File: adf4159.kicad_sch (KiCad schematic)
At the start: 0 parts

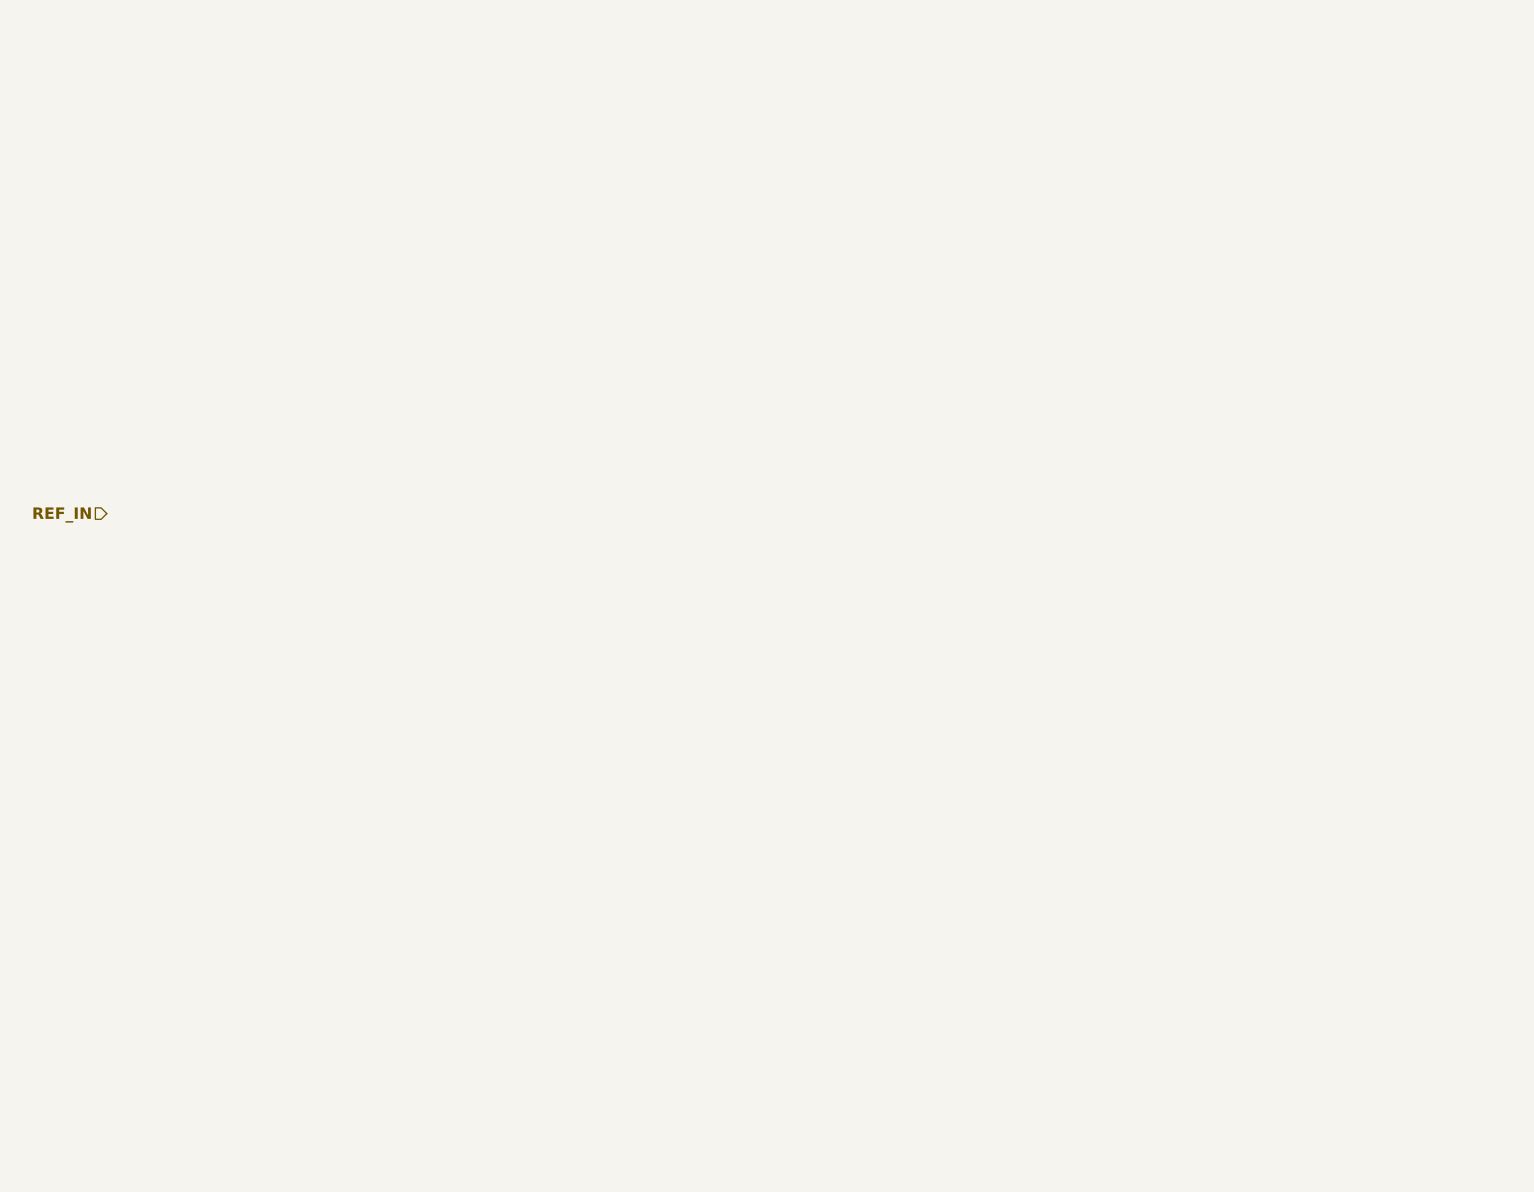
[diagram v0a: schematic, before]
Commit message: Complete Schematic of the PCB
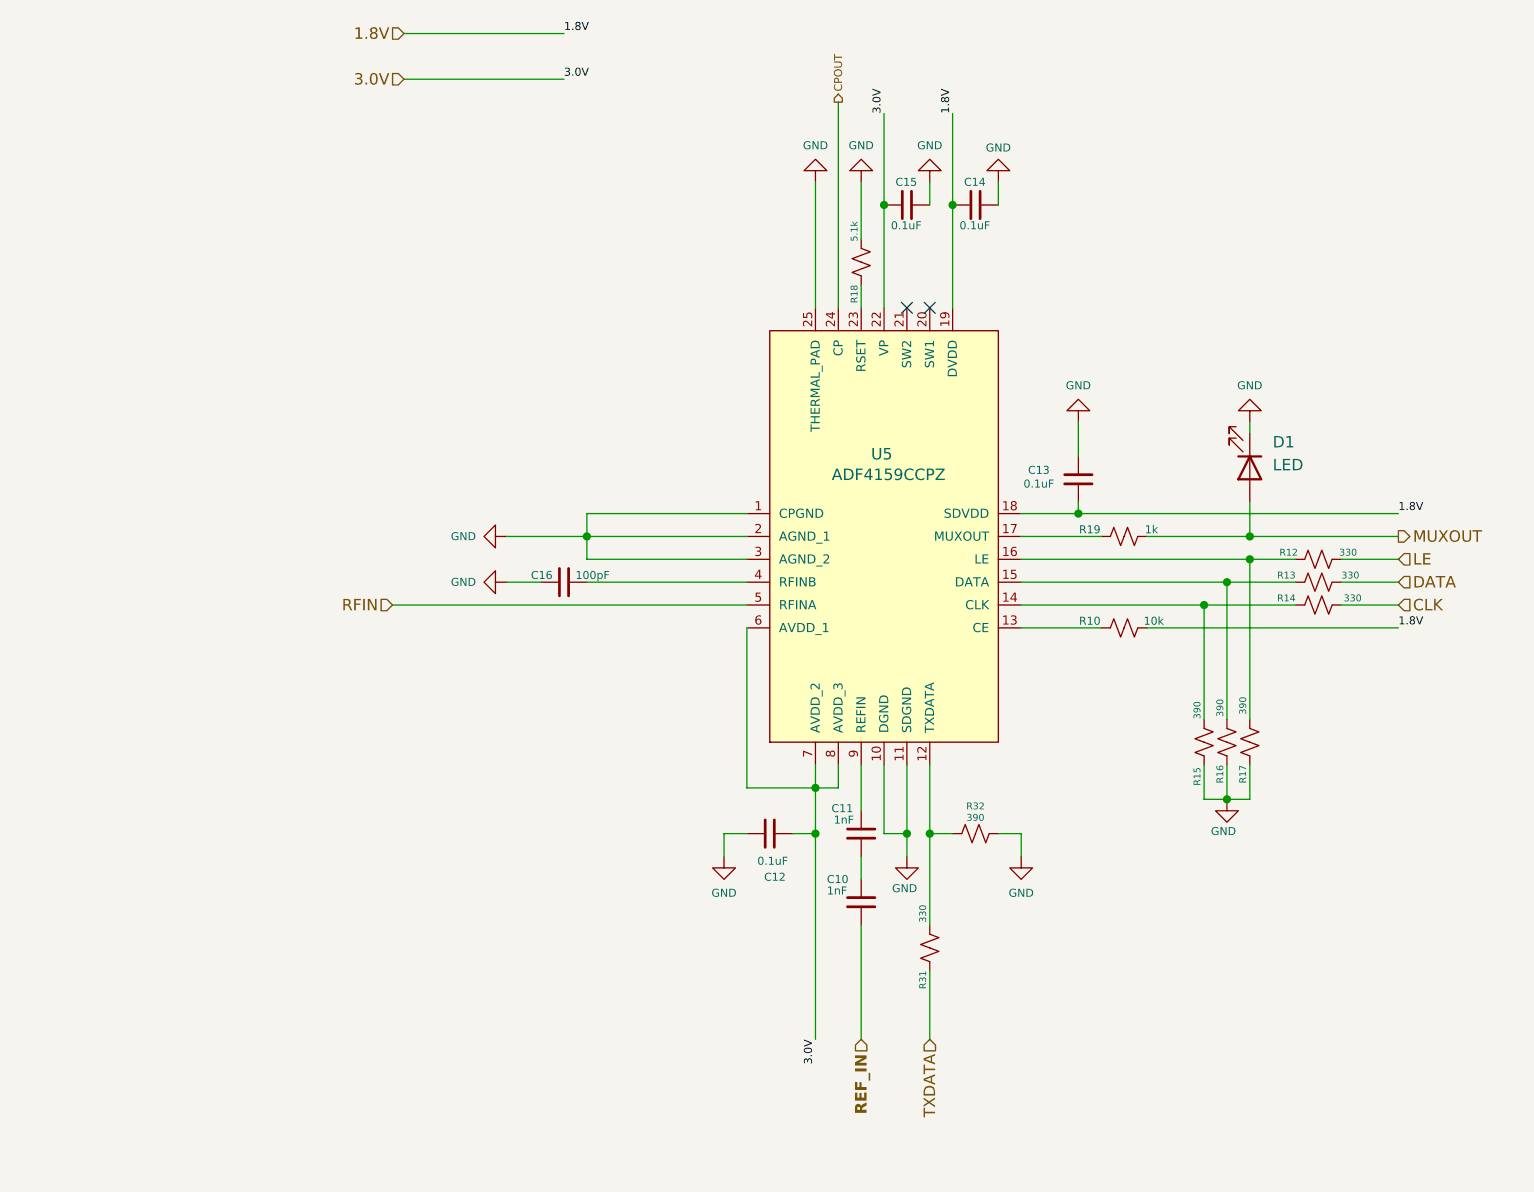
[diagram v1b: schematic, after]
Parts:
- added C10, C11: 1nF, Capacitor_SMD:C_0402_1005Metric_Pad0.74x0.62mm_HandSolder, symbol Device:C_Small
- added C12, C13, C14, C15: 0.1uF, Capacitor_SMD:C_0402_1005Metric_Pad0.74x0.62mm_HandSolder, symbol Device:C_Small
- added C16: 100pF, Capacitor_SMD:C_0402_1005Metric_Pad0.74x0.62mm_HandSolder, symbol Device:C_Small
- added D1: LED, LED_SMD:LED_0805_2012Metric, symbol Device:LED
- added R10: 10k, symbol Device:R_Small_US
- added R12, R13, R14, R31: 330, symbol Device:R_Small_US
- added R15, R16, R17, R32: 390, symbol Device:R_Small_US
- added R18: 5.1k, symbol Device:R_Small_US
- added R19: 1k, symbol Device:R_Small_US
- added U5: ADF4159CCPZ, ADF4159CCPZ:ADF4159CCPZ, symbol ADF4159CCPZ_PLL_Synthesizer:ADF4159CCPZ
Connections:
- net REF_IN: now also C10.2
- new net: R31.2, R32.1, U5.12 (TXDATA)
- new net: C11.1, U5.9 (REFIN)
- new net: C10.1, C11.2
- new net: R10.1, U5.13 (CE)
- new net: R14.1, R15.2, U5.14 (CLK)
- new net: R13.1, R16.2, U5.15 (DATA)
- new net: R12.1, R17.2, U5.16 (LE)
- new net: R19.1, U5.17 (MUXOUT)
- new net: R18.2, U5.23 (RSET)
- new net: C16.2, U5.4 (RFINB)
- new net 1.8V: C13.2, C14.2, R10.2, U5.18 (SDVDD), U5.19 (DVDD)
- new net 3.0V: C12.2, C15.2, U5.22 (VP), U5.6 (AVDD_1), U5.7 (AVDD_2), U5.8 (AVDD_3)
- new net CLK: R14.2
- new net CPOUT: U5.24 (CP)
- new net DATA: R13.2
- new net GND: C12.1, C13.1, C14.1, C15.1, C16.1, D1.1 (K), R15.1, R16.1, R17.1, R18.1, R32.2, U5.1 (CPGND), U5.10 (DGND), U5.11 (SDGND), U5.2 (AGND_1), U5.25 (THERMAL_PAD), U5.3 (AGND_2)
- new net LE: R12.2
- new net MUXOUT: D1.2 (A), R19.2
- new net RFIN: U5.5 (RFINA)
- new net TXDATA: R31.1
- no-connect marks 0 -> 2
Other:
- title: (none) -> ADF4159 PLL Synthesizer

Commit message: Remove 0ohm resistors for EN pins and SMA connector for external REFIN
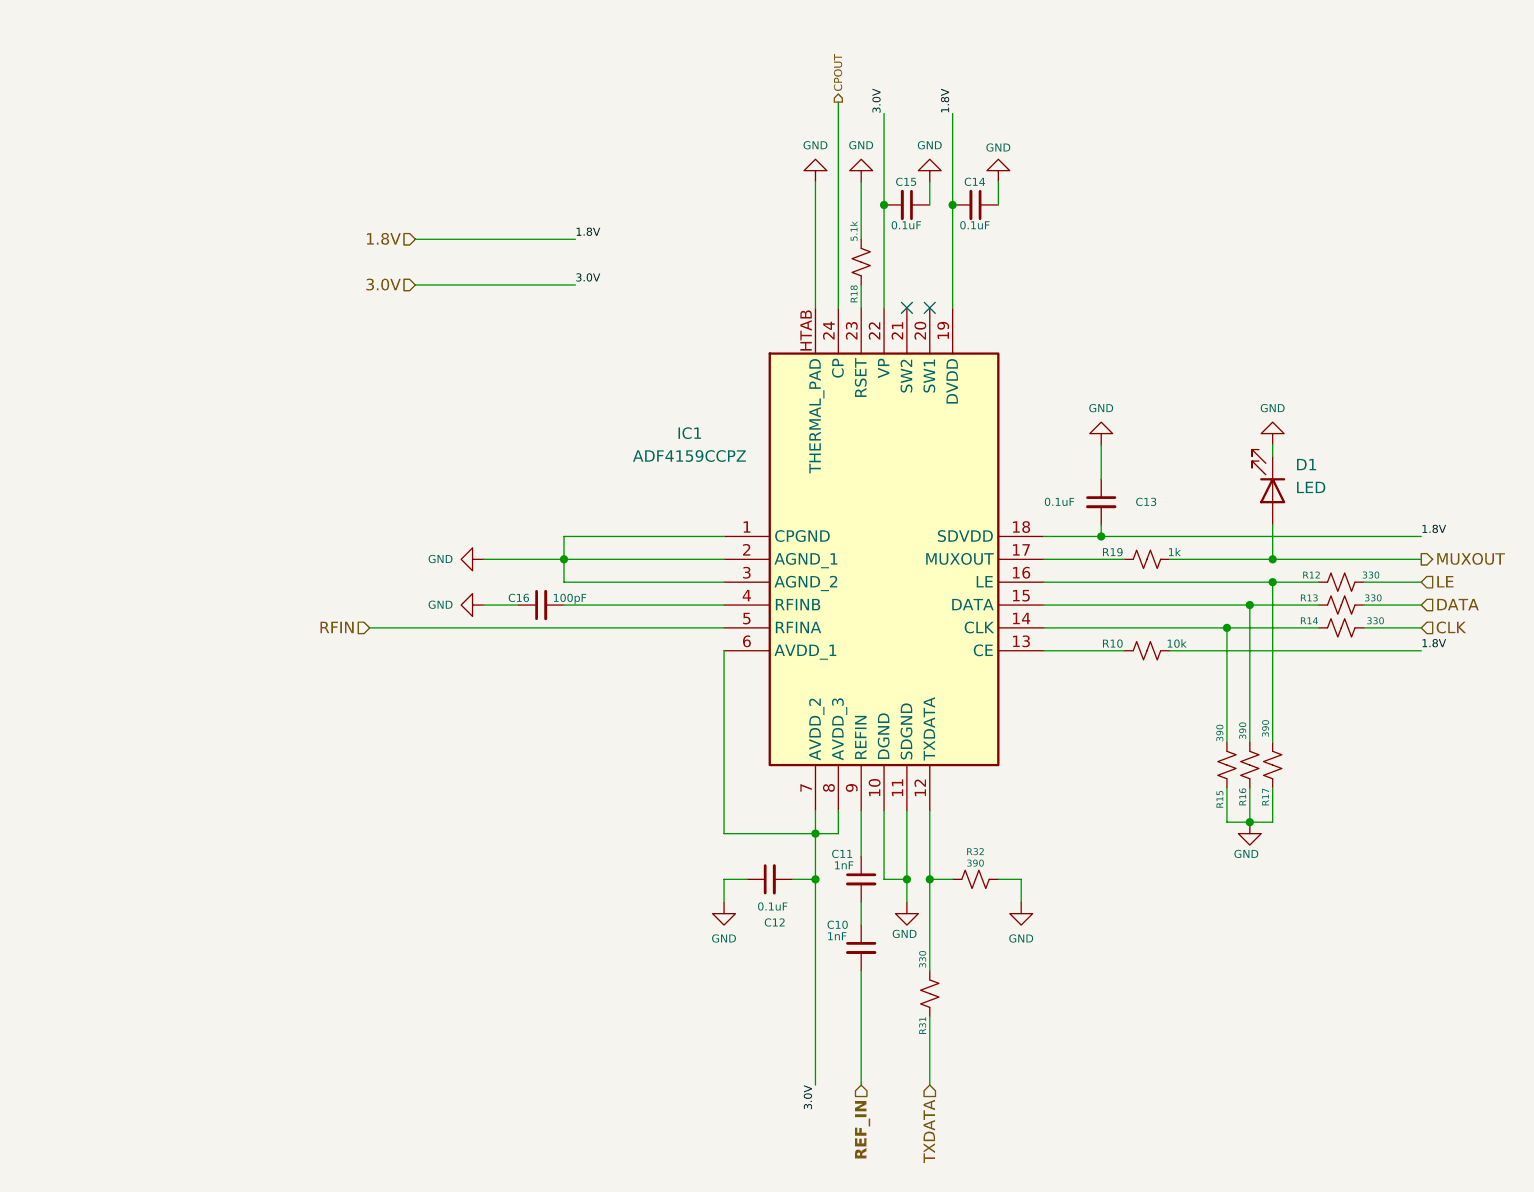
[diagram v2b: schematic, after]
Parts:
- removed U5: ADF4159CCPZ, ADF4159CCPZ:ADF4159CCPZ, symbol ADF4159CCPZ_PLL_Synthesizer:ADF4159CCPZ
- added IC1: ADF4159CCPZ, ADF4159:CP_24_10_ADI-L, symbol ADF4159CCPZ:ADF4159CCPZ
- C10, C11, C12, C13, C14, C15, C16: footprint Capacitor_SMD:C_0402_1005Metric_Pad0.74x0.62mm_HandSolder -> Capacitor_SMD:C_0402_1005Metric
- R10, R12, R13, R14, R15, R16, R17, R18, R19, R31, R32: footprint (none) -> Capacitor_SMD:C_0402_1005Metric
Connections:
- net 1.8V: now also IC1.18 (SDVDD), IC1.19 (DVDD)
- net 3.0V: now also IC1.22 (VP), IC1.6 (AVDD_1), IC1.7 (AVDD_2), IC1.8 (AVDD_3)
- net CPOUT: now also IC1.24 (CP)
- net GND: now also IC1.1 (CPGND), IC1.10 (DGND), IC1.11 (SDGND), IC1.2 (AGND_1), IC1.3 (AGND_2), IC1.HTAB (THERMAL_PAD)
- net RFIN: now also IC1.5 (RFINA)
- net at R31.2, R32.1: now also IC1.12 (TXDATA)
- net at C11.1: now also IC1.9 (REFIN)
- net at R10.1: now also IC1.13 (CE)
- net at R14.1, R15.2: now also IC1.14 (CLK)
- net at R13.1, R16.2: now also IC1.15 (DATA)
- net at R12.1, R17.2: now also IC1.16 (LE)
- net at R19.1: now also IC1.17 (MUXOUT)
- net at R18.2: now also IC1.23 (RSET)
- net at C16.2: now also IC1.4 (RFINB)
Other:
- moved on the sheet: C10, C11, C12, C13, C16, D1, R10, R12, R13, R14, R15, R16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

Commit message: Complete and adjust the PCB based on advisor's advice and manufacturer in-stock parts
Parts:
- R10, R12, R13, R14, R15, R16, R17, R18, R19, R31, R32: footprint Capacitor_SMD:C_0402_1005Metric -> Resistor_SMD:R_0402_1005Metric
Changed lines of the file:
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@@
 			)
 		)
-		(property "Footprint" "Capacitor_SMD:C_0402_1005Metric"
+		(property "Footprint" "Resistor_SMD:R_0402_1005Metric"
 			(at 153.67 127 0)
 			(hide yes)
@@
 			)
 		)
-		(property "Footprint" "Capacitor_SMD:C_0402_1005Metric"
+		(property "Footprint" "Resistor_SMD:R_0402_1005Metric"
 			(at 181.61 114.3 0)
 			(hide yes)
@@
 			)
 		)
-		(property "Footprint" "Capacitor_SMD:C_0402_1005Metric"
+		(property "Footprint" "Resistor_SMD:R_0402_1005Metric"
 			(at 172.72 91.44 0)
 			(hide yes)
@@
 			)
 		)
-		(property "Footprint" "Capacitor_SMD:C_0402_1005Metric"
+		(property "Footprint" "Resistor_SMD:R_0402_1005Metric"
 			(at 148.59 139.7 0)
 			(hide yes)
@@
 			)
 		)
-		(property "Footprint" "Capacitor_SMD:C_0402_1005Metric"
+		(property "Footprint" "Resistor_SMD:R_0402_1005Metric"
 			(at 194.31 93.98 0)
 			(hide yes)
@@
 			)
 		)
-		(property "Footprint" "Capacitor_SMD:C_0402_1005Metric"
+		(property "Footprint" "Resistor_SMD:R_0402_1005Metric"
 			(at 194.31 96.52 0)
 			(hide yes)
@@
 			)
 		)
-		(property "Footprint" "Capacitor_SMD:C_0402_1005Metric"
+		(property "Footprint" "Resistor_SMD:R_0402_1005Metric"
 			(at 172.72 101.6 0)
 			(hide yes)
@@
 			)
 		)
-		(property "Footprint" "Capacitor_SMD:C_0402_1005Metric"
+		(property "Footprint" "Resistor_SMD:R_0402_1005Metric"
 			(at 186.69 114.3 0)
 			(hide yes)
@@
 			)
 		)
-		(property "Footprint" "Capacitor_SMD:C_0402_1005Metric"
+		(property "Footprint" "Resistor_SMD:R_0402_1005Metric"
 			(at 140.97 58.42 0)
 			(hide yes)
@@
 			)
 		)
-		(property "Footprint" "Capacitor_SMD:C_0402_1005Metric"
+		(property "Footprint" "Resistor_SMD:R_0402_1005Metric"
 			(at 194.31 99.06 0)
 			(hide yes)
@@
 			)
 		)
-		(property "Footprint" "Capacitor_SMD:C_0402_1005Metric"
+		(property "Footprint" "Resistor_SMD:R_0402_1005Metric"
 			(at 184.15 114.3 0)
 			(hide yes)
